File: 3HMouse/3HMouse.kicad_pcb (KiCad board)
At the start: 2 copper layers, 123.8 x 138.1 mm, 117 parts, among them J1 USB_C_Receptacle_USB2.0, SW0_0 CherryMX, SW0_1 CherryMX, SW0_2 CherryMX, SW1_0 CherryMX, SW1_1 CherryMX, SW1_2 CherryMX, SW2_0 CherryMX, SW2_1 CherryMX, SW2_2 CherryMX, SW3_0 CherryMX, SW3_1 CherryMX, SW3_2 CherryMX, SW3_3 CherryMX, SW3_4 CherryMX, SW4_0 CherryMX, SW4_1 CherryMX, SW4_2 CherryMX, SW4_3 CherryMX, SW4_4 CherryMX, SW5_0 CherryMX, SW5_1 CherryMX, SW5_2 CherryMX, SW5_3 CherryMX, SW5_4 CherryMX, SW6_0 CherryMX, SW6_1 CherryMX, SW6_2 CherryMX, SW6_3 CherryMX, SW6_4 CherryMX, U1 ATmega32U4-M, U2 USBLC6-2SC6, Y1 16 MHz

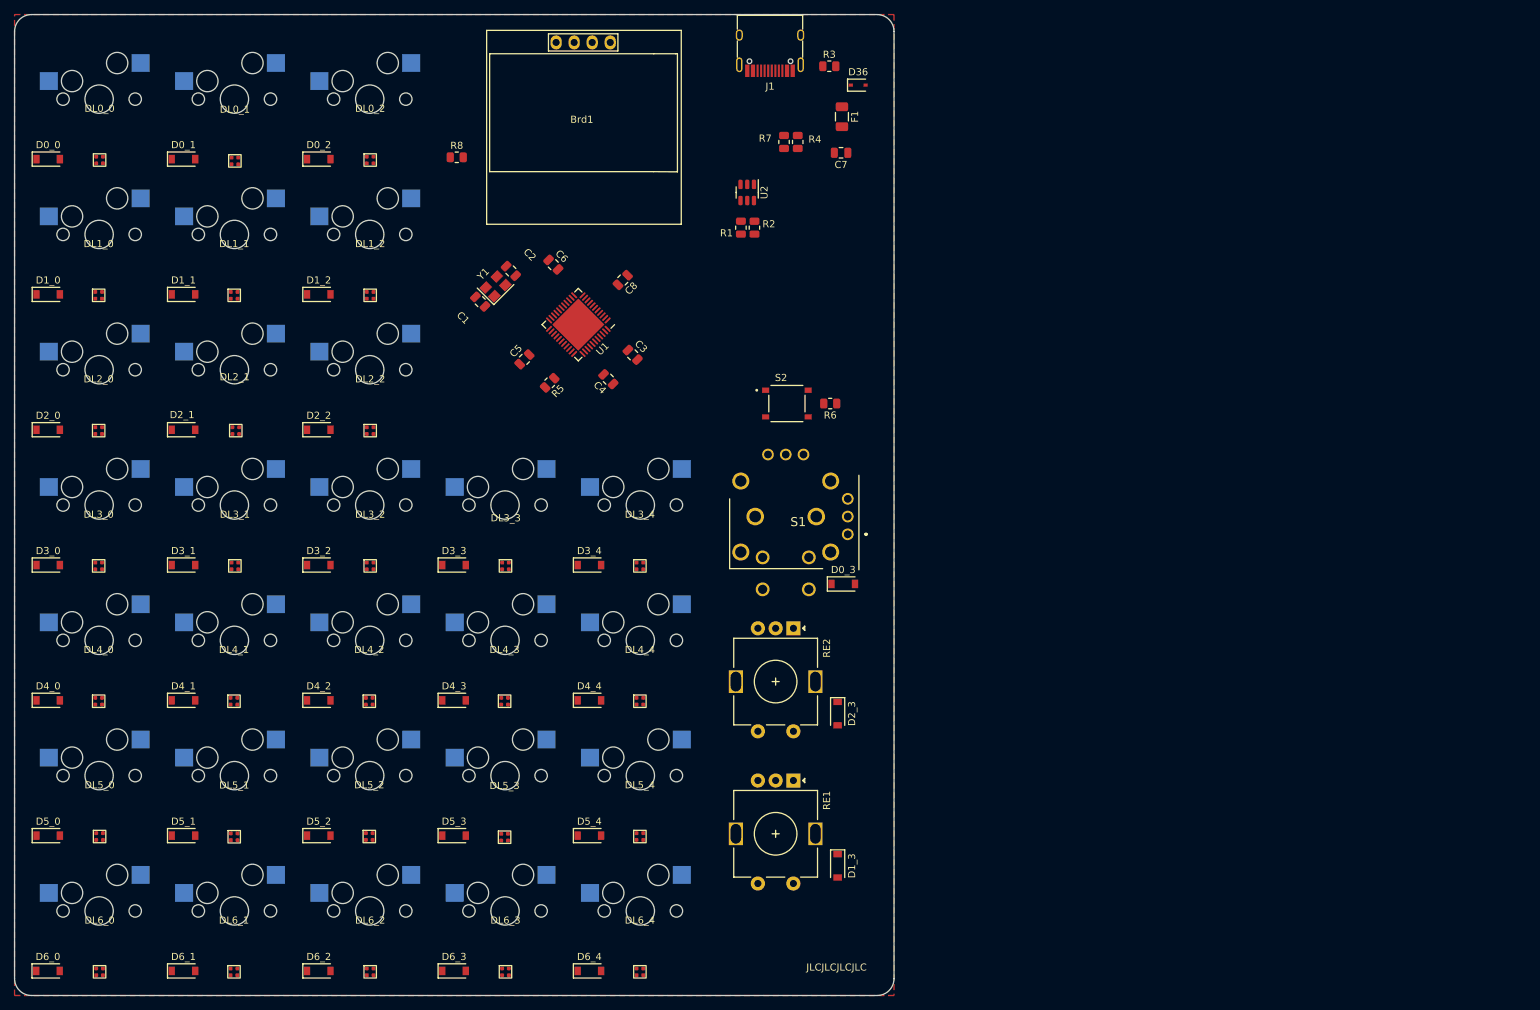
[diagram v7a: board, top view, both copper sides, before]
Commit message: LED and switch routing
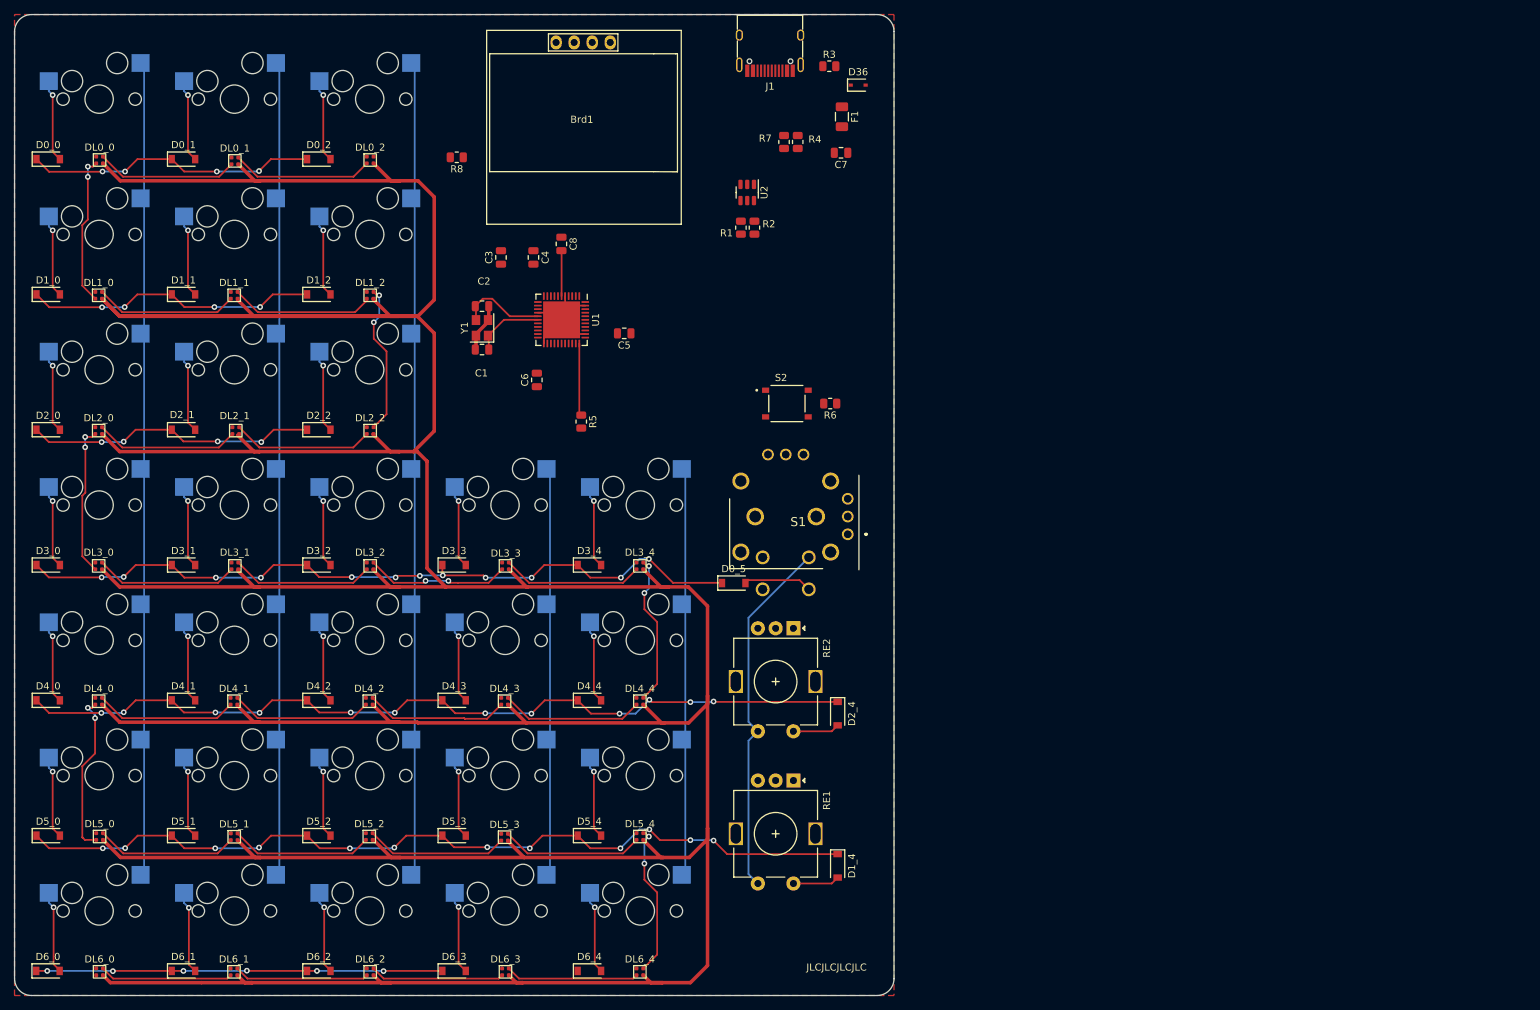
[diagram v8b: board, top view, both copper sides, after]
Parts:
- moved C3 23.1 mm to (89.9, 55.6), turned to 90 degrees
- moved C4 20.1 mm to (94.5, 55.6), turned to -90 degrees
- moved C6 16.4 mm to (95.0, 72.9), turned to 90 degrees
- moved D0_5 15.4 mm to (122.7, 101.5)
- moved C5 14.5 mm to (107.3, 66.3), turned to 180 degrees
- moved C8 10.0 mm to (98.4, 53.7), turned to -90 degrees
- moved R5 7.04 mm to (101.2, 78.7), turned to -90 degrees
- moved C1 6.75 mm to (87.2, 68.6), turned to 180 degrees
- moved C2 6.41 mm to (87.2, 62.5), turned to 0 degrees
- moved Y1 6.16 mm to (87.2, 65.5), turned to 90 degrees
- moved U1 2.46 mm to (98.4, 64.4), turned to -90 degrees
- turned R8 to 180 degrees
- renumbered D0_3 to D0_5, D1_3 to D1_4, D2_3 to D2_4
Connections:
- net Net-(D36-Pad1) renamed /RAWPWR
- D0_5 pad 1: ROW0 -> ROW3
- D1_4 pad 1: ROW1 -> ROW5
- D2_4 pad 1: ROW2 -> ROW4
- DL0_0 pad 1: Net-(DL0_0-Pad1) -> Net-(DL1_0-Pad1)
- DL1_0 pad 1: Net-(DL0_2-Pad3) -> Net-(DL1_0-Pad1)
- DL2_0 pad 1: Net-(DL1_2-Pad3) -> Net-(DL2_0-Pad1)
- DL2_2 pad 3: Net-(DL2_2-Pad3) -> Net-(DL1_2-Pad3)
- DL3_0 pad 1: Net-(DL2_2-Pad3) -> Net-(DL2_0-Pad1)
- DL3_4 pad 3: Net-(DL3_4-Pad3) -> Net-(DL4_4-Pad3)
- DL4_0 pad 1: Net-(DL3_4-Pad3) -> Net-(DL4_0-Pad1)
- DL5_0 pad 1: Net-(DL4_4-Pad3) -> Net-(DL4_0-Pad1)
- DL5_4 pad 3: Net-(DL5_4-Pad3) -> Net-(DL6_4-Pad3)
- DL6_0 pad 1: Net-(DL5_4-Pad3) -> unconnected-(DL6_0-Pad1)
- DL6_4 pad 3: unconnected-(DL6_4-Pad3) -> Net-(DL6_4-Pad3)
- R8 pad 1: LED -> Net-(DL0_2-Pad3)
- R8 pad 2: Net-(DL0_0-Pad1) -> LED
- RE1 pad S1: COL3 -> COL5
- RE2 pad S1: COL3 -> COL5
- S1 pad C1: COL3 -> COL5
- U1 pad 1: unconnected-(U1-Pad1) -> LED
- U1 pad 11: COL0 -> ROW0
- U1 pad 12: ROW2 -> unconnected-(U1-Pad12)
- U1 pad 18: LED -> ROW2
- U1 pad 26: unconnected-(U1-Pad26) -> COL5
- U1 pad 9: ROW0 -> COL0
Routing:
- net +5V: track 0.00 -> 732.7 mm
- net ROW5: track 0.00 -> 122.0 mm, vias 0 -> 12
- net ROW4: track 0.00 -> 120.5 mm, vias 0 -> 12
- net COL2: track 0.00 -> 116.7 mm
- net COL1: track 0.00 -> 116.7 mm
- net COL0: track 0.00 -> 116.7 mm
- net ROW3: track 0.00 -> 105.9 mm, vias 0 -> 12
- net COL3: track 0.00 -> 58.4 mm
- net COL4: track 0.00 -> 58.4 mm
- net ROW6: track 0.00 -> 57.3 mm, vias 0 -> 6
- net COL5: track 0.00 -> 51.1 mm
- net ROW1: track 0.00 -> 41.1 mm, vias 0 -> 4
- net ROW0: track 0.00 -> 41.0 mm, vias 0 -> 4
- net ROW2: track 0.00 -> 41.0 mm, vias 0 -> 4
- net GND: track 0.00 -> 26.9 mm
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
